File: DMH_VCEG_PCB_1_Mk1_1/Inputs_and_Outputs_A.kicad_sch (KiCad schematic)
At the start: 45 parts, among them J1 TS_Jack_6.35mm_Sw, J10 TS_Jack_6.35mm_Sw, J2 TS_Jack_6.35mm_Sw, J200 IDC_02x08, J21 Conn_01x10_PinHeader, J22 Conn_01x10_PinHeader, J23 Conn_01x10_PinHeader, J24 Conn_01x06_PinHeader, J3 TS_Jack_6.35mm_Sw, J4 TS_Jack_6.35mm_Sw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

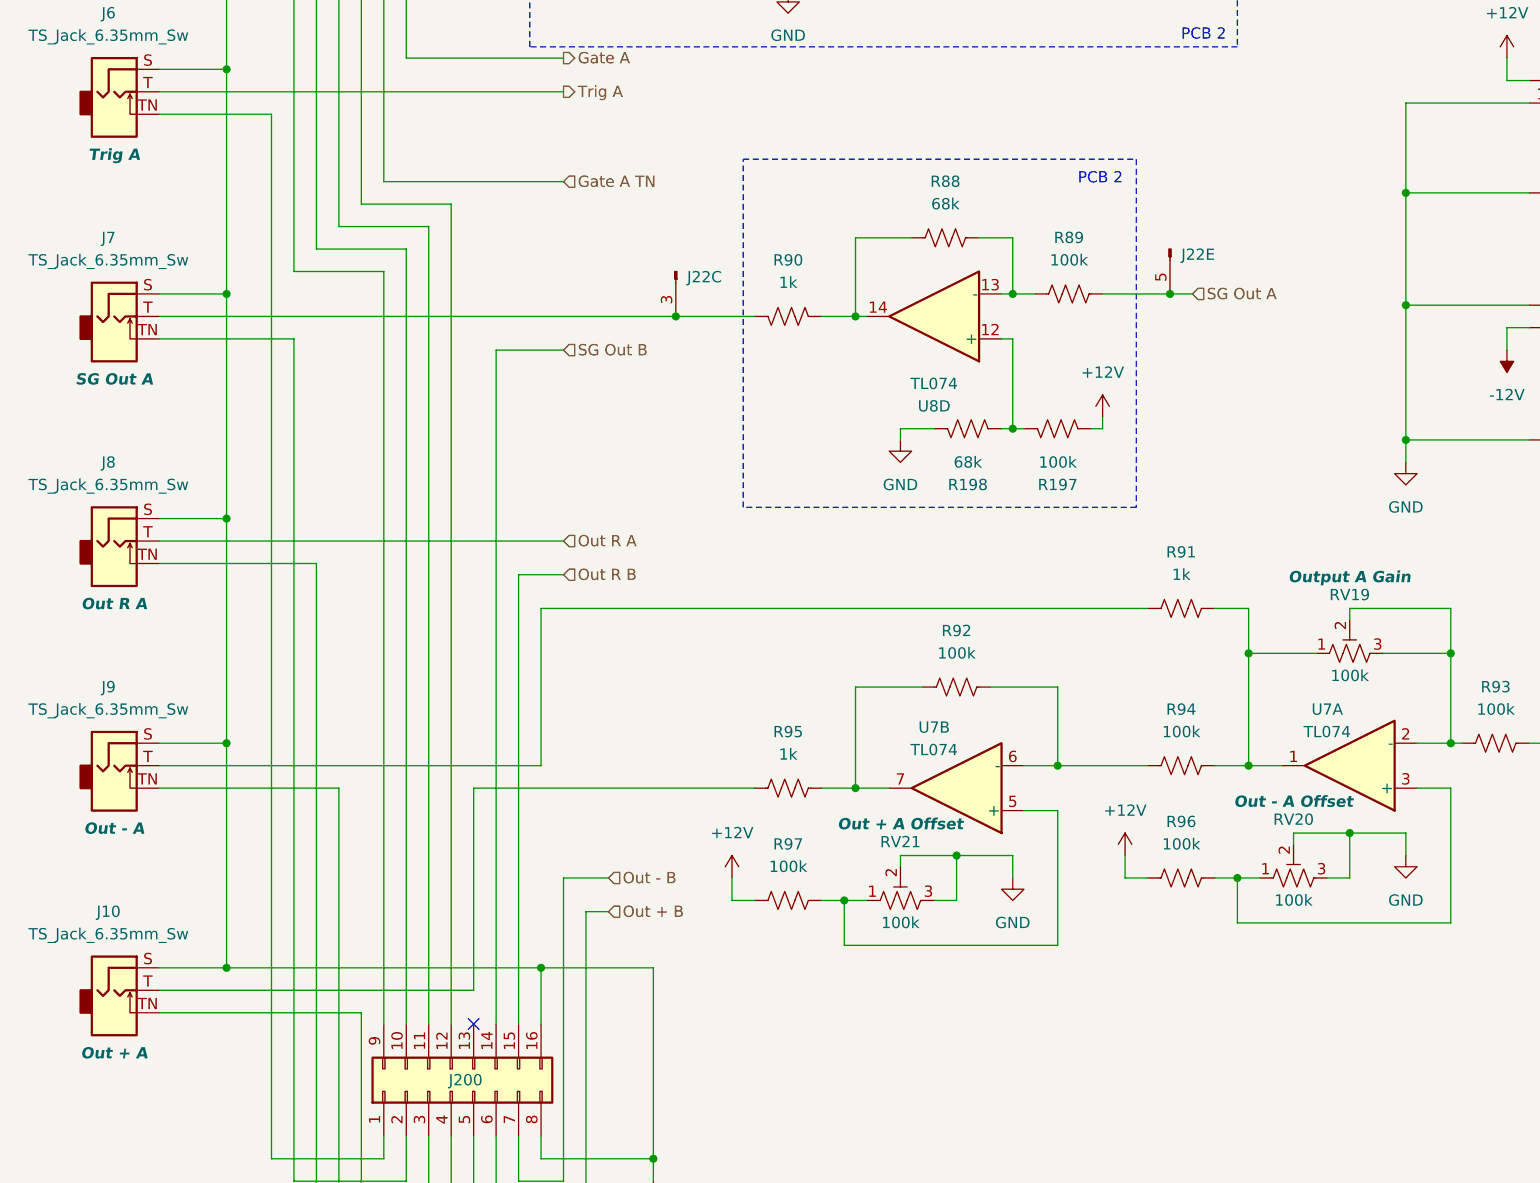
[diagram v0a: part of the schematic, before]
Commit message: Added diodes to Sustain Gate outputs
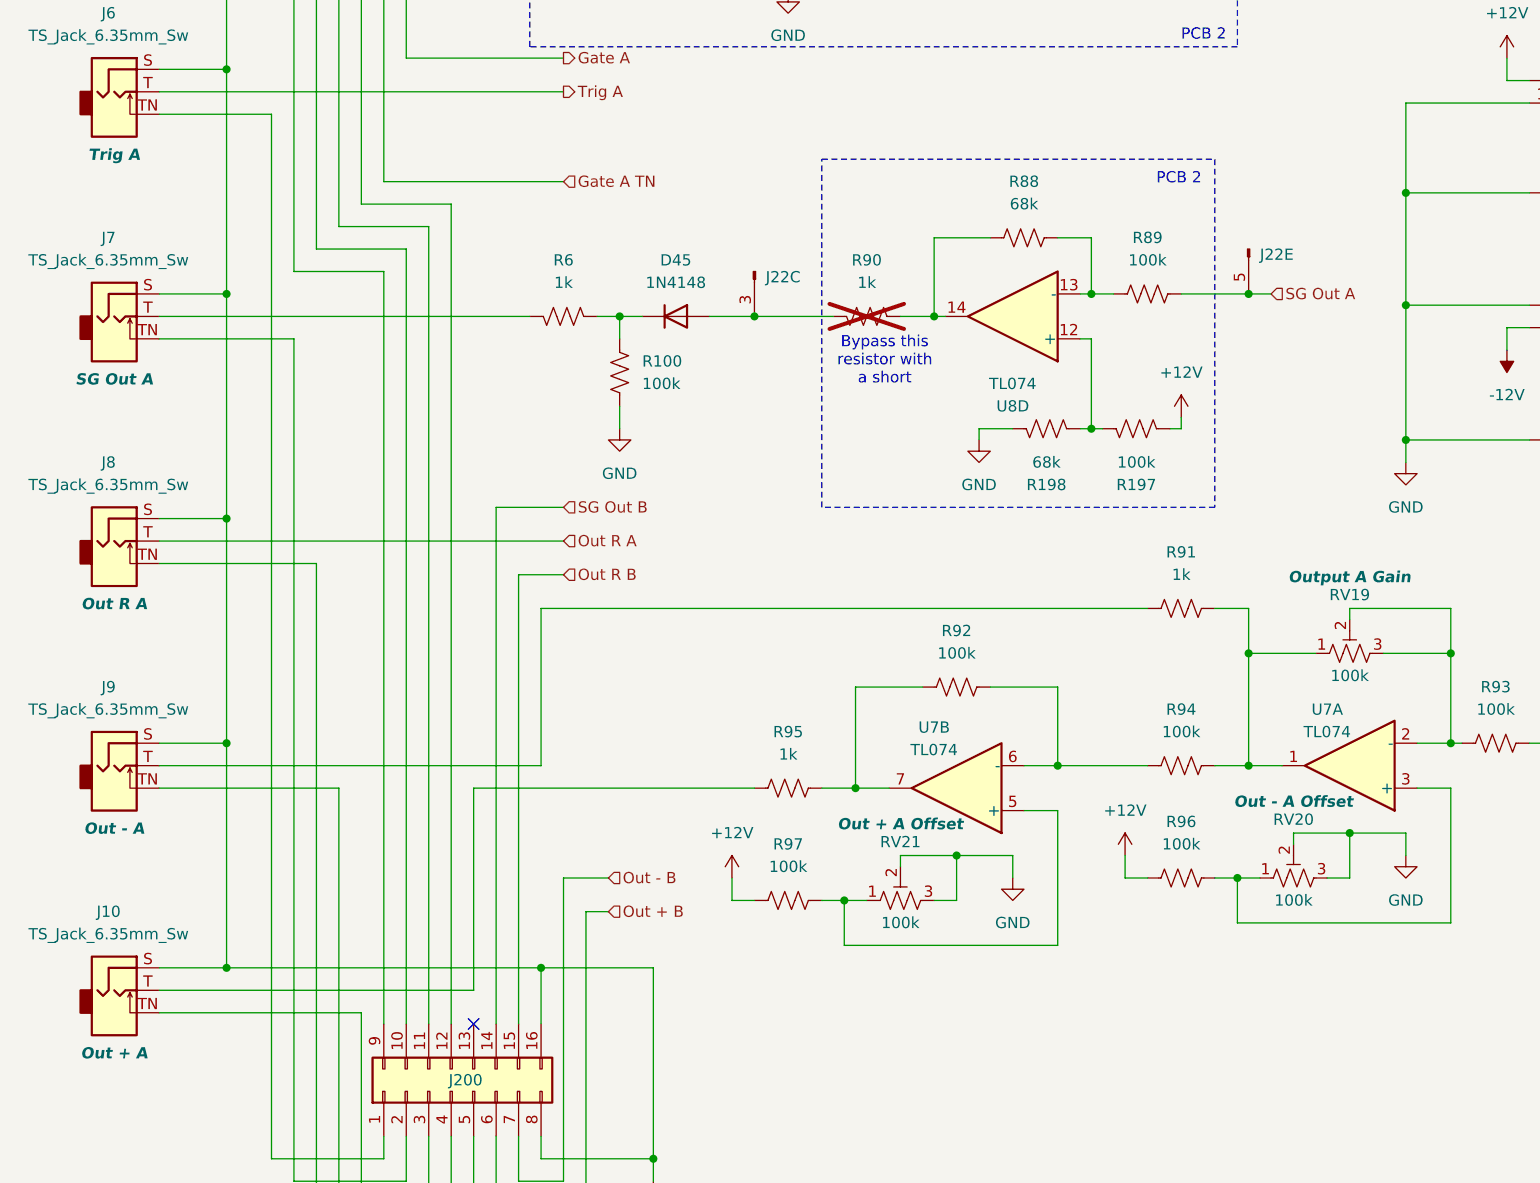
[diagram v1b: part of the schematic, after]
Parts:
- added D45: 1N4148, Diode_THT:D_DO-35_SOD27_P7.62mm_Horizontal, symbol Diode:1N4148
- added R100: 100k, Resistor_THT:R_Axial_DIN0207_L6.3mm_D2.5mm_P7.62mm_Horizontal, symbol Device:R_US
- added R6: 1k, Resistor_THT:R_Axial_DIN0207_L6.3mm_D2.5mm_P7.62mm_Horizontal, symbol Device:R_US
- R90: now not fitted
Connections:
- net GND: now also R100.2
- net at J22.3 (Pin_3), R90.1: now also D45.2 (A); no longer J7.T
- new net: D45.1 (K), R100.1, R6.2
- new net: J7.T, R6.1
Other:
- note added: "Bypass this resistor with a short"
- moved on the sheet: J22C, J22E, R197, R198, R88, R89, U8D
